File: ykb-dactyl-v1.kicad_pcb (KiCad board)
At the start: 2 copper layers, 55.8 x 58.3 mm, 58 parts, among them IC1 TXU0101DCKR, J1 JST_SH_BM10B-SRSS-TB_1x10-1MP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, J2 JST_SH_BM10B-SRSS-TB_1x10-1MP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, J3 JST_SH_BM10B-SRSS-TB_1x10-1MP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, J4 JST_SH_BM10B-SRSS-TB_1x10-1MP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, J5 JST_SH_BM10B-SRSS-TB_1x10-1MP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, J6 JST_SH_BM10B-SRSS-TB_1x10-1MP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, J7 JST_SH_BM12B-SRSS-TB_1x12-1MP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, J8 MC-121-L124, J9 Conn_ARM_SWD_TagConnect_TC203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

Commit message: Update
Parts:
- removed C1: C, Capacitor_SMD:C_0402_1005Metric
- removed the R1 at (104.9, 94.4)
- added D2: QLS6B-FKW, LED_SMD:LED_Cree-PLCC6_4.7x1.5mm, F.Cu at (114.1, 86.0)
- added J10: Conn_01x05, Connector_PinSocket_2.54mm:PinSocket_1x05_P2.54mm_Vertical, F.Cu at (70.0, 96.0)
- added R4: 10K, Resistor_SMD:R_0402_1005Metric, F.Cu at (64.5, 29.5)
- added R5: 10K, Resistor_SMD:R_0402_1005Metric, F.Cu at (59.2, 33.1)
- added R6: 10K, Resistor_SMD:R_0402_1005Metric, F.Cu at (59.2, 35.1)
- added S6: SKRTLAE010, footprints:SKRTLAE010, F.Cu at (112.2, 79.5)
- J9: value Conn_ARM_SWD_TagConnect_TC2030_NL -> Conn_01x05; footprint Connector:Tag-Connect_TC2030-IDC-NL_2x03_P1.27mm_Vertical -> Connector_PinSocket_2.54mm:PinSocket_1x05_P2.54mm_Vertical; moved to F.Cu
- R1, R2, R3: value 1K -> 600
- moved J9 25.1 mm to (102.3, 97.0)
- moved D1 19.7 mm to (65.6, 85.5), turned to -101.988 degrees
- moved S3 14.0 mm to (93.8, 77.8)
- moved S5 10.4 mm to (67.8, 79.0), turned to -101.988 degrees
- moved S4 7.70 mm to (78.2, 79.3)
- moved S1 6.91 mm to (78.8, 73.3)
- moved J7 4.05 mm to (90.0, 63.0)
- moved J6 3.80 mm to (98.0, 62.5)
- moved J5 3.55 mm to (82.0, 63.0)
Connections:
- net Net-(D1-KB) renamed /MCU/DBG_LED_P
- net Net-(D1-KR-Pad4) renamed /MCU/BAT_STAT_1_P
- net Net-(D1-KR-Pad6) renamed /MCU/BAT_STAT_2_P
- J9 pad 1: +3.3V_SYS -> /MCU/DBG_UART_APPCORE_TX
- J9 pad 2: /MCU/SWDIO -> /MCU/DBG_UART_APPCORE_RX
- J9 pad 3: /MCU/RESET -> /MCU/DBG_UART_NETCORE_TX
- J9 pad 4: /MCU/SWCLK -> /MCU/DBG_UART_NETCORE_RX
- U1 pad P1.2: /MCU/I2C_SDA -> unconnected-(U1B-P1.02-PadP1.2)
- U1 pad P1.4: /MCU/I2C_SCL -> unconnected-(U1B-P1.04-PadP1.4)

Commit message: Update
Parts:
- added D3: RB751S40,115, footprints:RB751S40115, F.Cu at (58.5, 48.6)
- added R23: 47K, Resistor_SMD:R_0402_1005Metric, F.Cu at (57.5, 51.5)
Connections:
- U1 pad P0.13: unconnected-(U1-PadP0.13) -> /MCU/SW_P

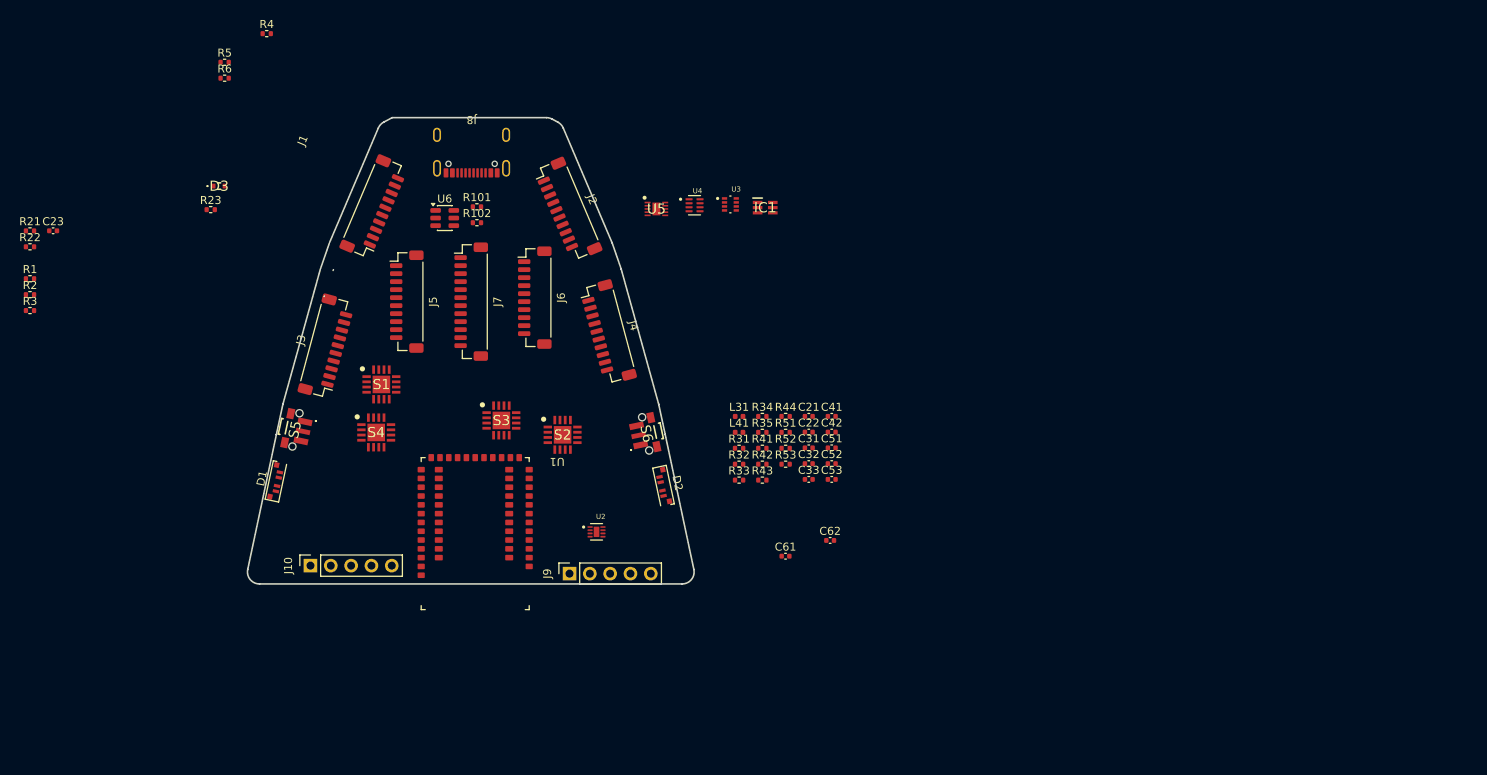
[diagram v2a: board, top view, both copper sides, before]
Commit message: Fix board shape
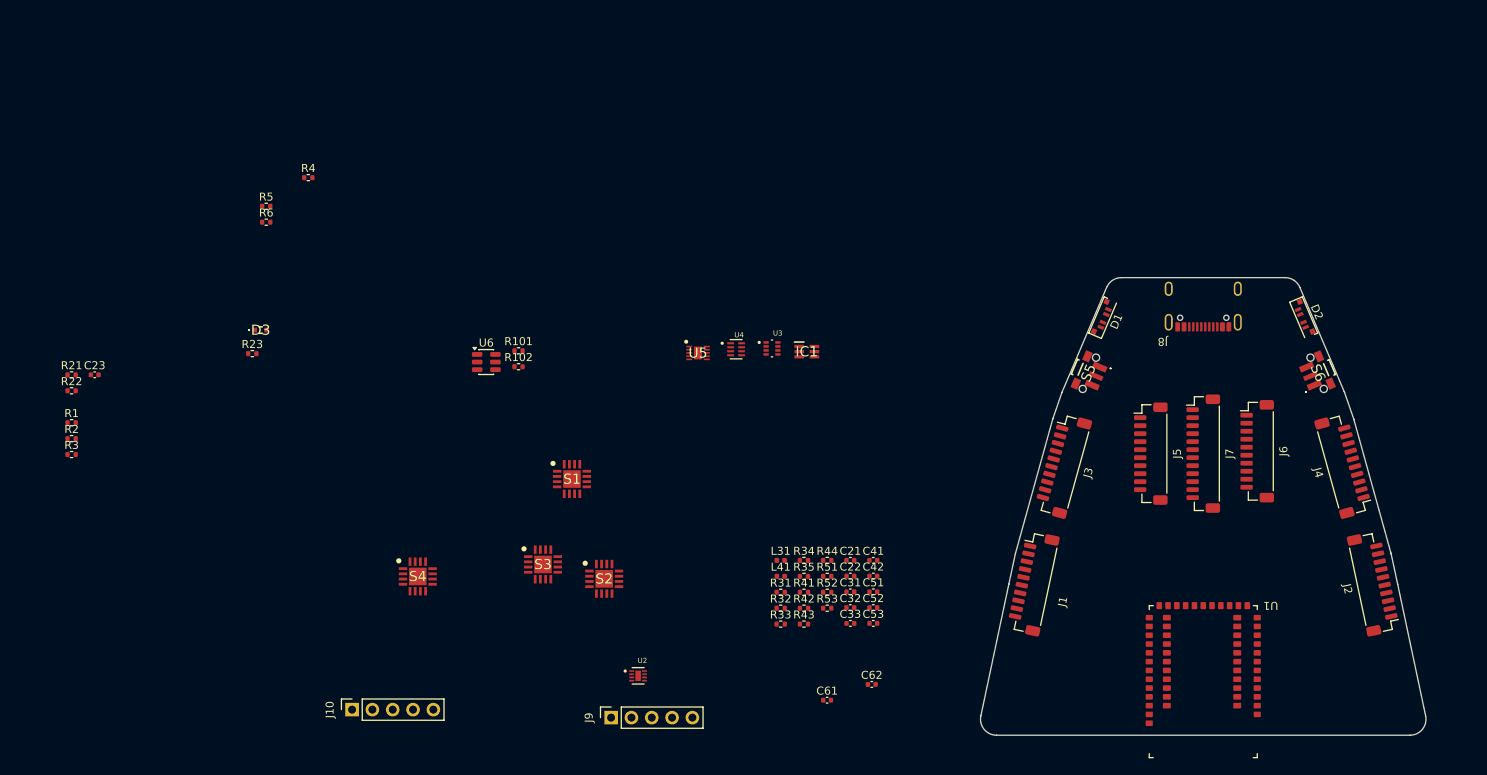
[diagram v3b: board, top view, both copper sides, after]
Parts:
- U1: value holyiot-21069 -> Holyiot-21069
- moved J2 111.0 mm to (202.8, 98.2), turned to 101.989 degrees
- moved D1 105.4 mm to (169.0, 65.0), turned to -113.058 degrees
- moved S5 99.5 mm to (167.0, 71.8), turned to -113.058 degrees
- moved J5 94.9 mm to (175.0, 82.0)
- moved J1 94.8 mm to (160.3, 98.2), turned to -101.988 degrees
- moved J8 94.4 mm to (181.6, 63.0)
- moved J4 93.5 mm to (199.1, 83.5), turned to 105.502 degrees
- moved J7 93.5 mm to (181.6, 82.0)
- moved J3 93.2 mm to (164.0, 83.5), turned to -105.502 degrees
- moved J6 92.3 mm to (188.3, 81.7)
- moved U1 88.8 mm to (181.6, 110.5)
- moved S6 84.3 mm to (196.1, 71.8), turned to 113.058 degrees
- moved D2 82.7 mm to (194.1, 65.0), turned to 113.058 degrees
- moved S1 26.6 mm to (102.7, 85.2)
- moved D3 18.7 mm to (63.7, 66.6)
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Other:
- board size 55.8 x 58.3 mm -> 55.7 x 57.2 mm

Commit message: Fix global nets
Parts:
- U1: value Holyiot-21069 -> holyiot-21069
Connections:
- C23 pad 1: /Power/SHDN -> SHDN
- D3 pad 1: /Power/SW_P -> SW_P
- IC1 pad 4: /MCU/LED_D_0 -> LED_D_0
- J1 pad 5: /MUXes/MUX1_D -> MUX1_D
- J1 pad 7: /MUXes/LED_D_0 -> LED_D_0
- J2 pad 5: /MUXes/MUX1_D -> MUX1_D
- J3 pad 5: /MUXes/MUX2_D -> MUX2_D
- J4 pad 5: /MUXes/MUX2_D -> MUX2_D
- J5 pad 5: /MUXes/MUX3_D -> MUX3_D
- J6 pad 5: /MUXes/MUX3_D -> MUX3_D
- J7 pad 7: /MUXes/MUX4_D -> MUX4_D
- R1 pad 1: /MCU/BAT_STAT_1 -> BAT_STAT_1
- R2 pad 1: /MCU/BAT_STAT_2 -> BAT_STAT_2
- R21 pad 1: /Power/SHDN -> SHDN
- R23 pad 1: /Power/SW_P -> SW_P
- R4 pad 1: /MCU/BAT_STAT_1 -> BAT_STAT_1
- R5 pad 1: /MCU/BAT_STAT_2 -> BAT_STAT_2
- S1 pad 13: /MUXes/MUX1_D -> MUX1_D
- S1 pad 15: /MUXes/MUX1_A2 -> MUX1_A2
- S1 pad 5: /MUXes/MUX1_A0 -> MUX1_A0
- S1 pad 7: /MUXes/MUX1_A1 -> MUX1_A1
- S2 pad 13: /MUXes/MUX2_D -> unconnected-(S2-D-Pad13)
- S2 pad 15: /MUXes/MUX2_A2 -> MUX2_A2
- S2 pad 5: /MUXes/MUX2_A0 -> MUX2_A0
- S2 pad 7: /MUXes/MUX2_A1 -> MUX2_A1
- S3 pad 13: /MUXes/MUX3_D -> MUX3_D
- S3 pad 15: /MUXes/MUX3_A2 -> MUX3_A2
- S3 pad 5: /MUXes/MUX3_A0 -> MUX3_A0
- S3 pad 7: /MUXes/MUX3_A1 -> MUX3_A1
- S4 pad 13: /MUXes/MUX4_D -> MUX4_D
- S4 pad 15: /MUXes/MUX4_A2 -> MUX4_A2
- S4 pad 5: /MUXes/MUX4_A0 -> MUX4_A0
- S4 pad 7: /MUXes/MUX4_A1 -> MUX4_A1
- U1 pad D+: /MCU/USB_DP_P -> USB_DP_P
- U1 pad D-: /MCU/USB_DN_P -> USB_DN_P
- U1 pad P0.10: /MCU/MUX1_A2 -> MUX1_A2
- U1 pad P0.11: /MCU/MUX1_A1 -> MUX1_A1
- U1 pad P0.12: /MCU/MUX1_A0 -> MUX1_A0
- U1 pad P0.13: /MCU/SW_P -> SW_P
- U1 pad P0.14: /MCU/SHDN -> SHDN
- U1 pad P0.17: /MCU/BAT_STAT_1 -> BAT_STAT_1
- U1 pad P0.18: /MCU/BAT_STAT_2 -> BAT_STAT_2
- U1 pad P0.19: /MCU/MUX3_A1 -> MUX3_A1
- U1 pad P0.21: /MCU/MUX3_A0 -> MUX3_A0
- U1 pad P0.22: /MCU/MUX2_A1 -> MUX2_A1
- U1 pad P0.23: /MCU/MUX2_A2 -> MUX2_A2
- U1 pad P0.25: /MCU/MUX4_A0 -> MUX4_A0
- U1 pad P0.29: /MCU/MUX3_A2 -> MUX3_A2
- U1 pad P0.4: /MCU/MUX1_D -> MUX1_D
- U1 pad P0.5: /MCU/MUX2_D -> MUX2_D
- U1 pad P0.6: /MCU/MUX3_D -> MUX3_D
- U1 pad P0.7: /MCU/MUX4_D -> MUX4_D
- U1 pad P0.9: /MCU/MUX2_A0 -> MUX2_A0
- U1 pad P1.7: /MCU/MUX4_A2 -> MUX4_A2
- U1 pad P1.9: /MCU/MUX4_A1 -> MUX4_A1
- U2 pad 7: /Power/SHDN -> SHDN
- U5 pad 3: /Power/BAT_STAT_2 -> BAT_STAT_2
- U5 pad 9: /Power/BAT_STAT_1 -> BAT_STAT_1
- U6 pad 1: /USB/USB_DN_P -> USB_DN_P
- U6 pad 3: /USB/USB_DP_P -> USB_DP_P

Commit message: Place components
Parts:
- added J11: Conn_01x02_MountingPin, Connector_JST:JST_SH_BM02B-SRSS-TB_1x02-1MP_P1.00mm_Vertical, F.Cu at (184.3, 94.8)
- moved C23 155.1 mm to (197.9, 79.0)
- moved R21 155.1 mm to (195.0, 79.0)
- moved R22 155.1 mm to (195.0, 81.0)
- moved D3 137.1 mm to (199.7, 84.5)
- moved R23 137.1 mm to (198.7, 87.0)
- moved R1 134.0 mm to (174.0, 72.0)
- moved R2 134.0 mm to (174.0, 74.0)
- moved R3 134.0 mm to (174.0, 76.0)
- moved J10 124.5 mm to (198.9, 100.5), turned to 11.989 degrees
- moved R5 114.3 mm to (176.5, 73.5)
- moved R6 114.3 mm to (176.5, 75.5)
- moved R4 109.6 mm to (176.5, 72.0)
- moved J9 96.6 mm to (202.9, 99.6), turned to 11.989 degrees
- moved U2 91.8 mm to (198.3, 81.6)
- moved S4 91.8 mm to (175.2, 96.5)
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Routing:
- net GND: vias 0 -> 4

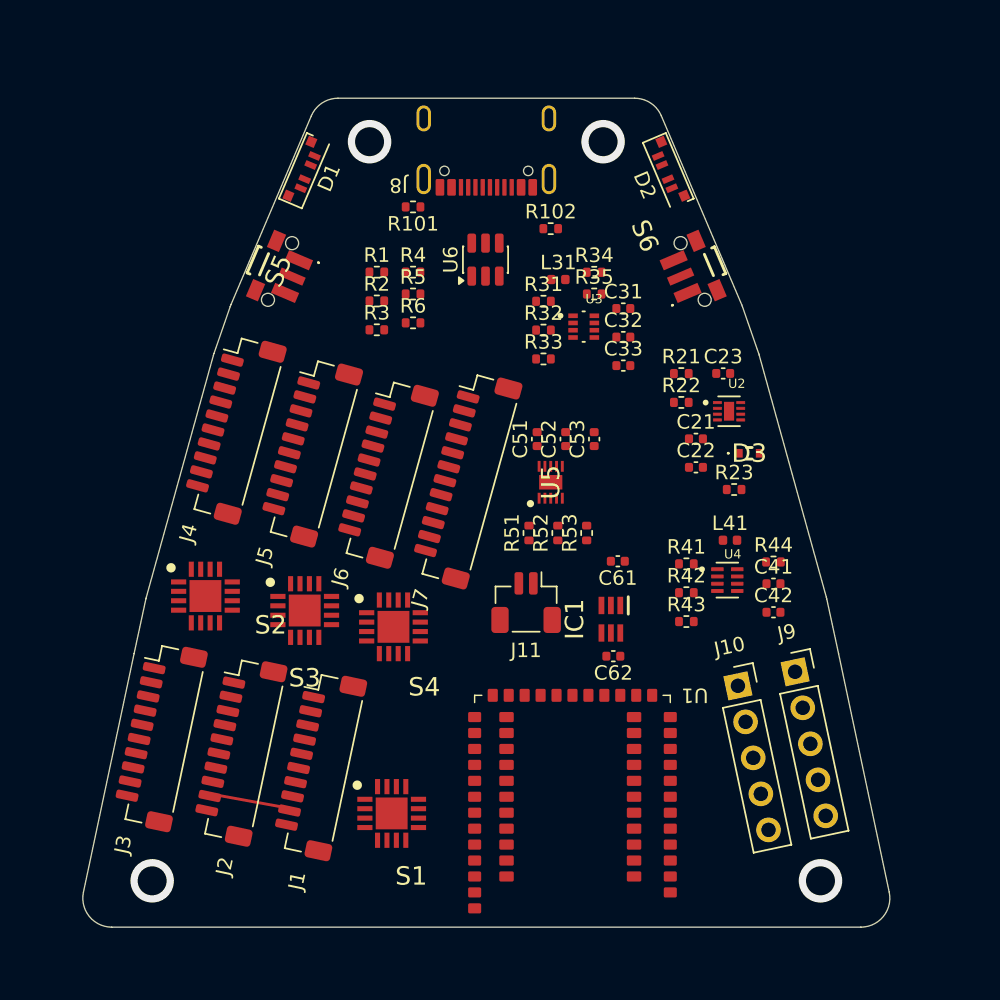
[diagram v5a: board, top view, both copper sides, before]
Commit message: Trace the board
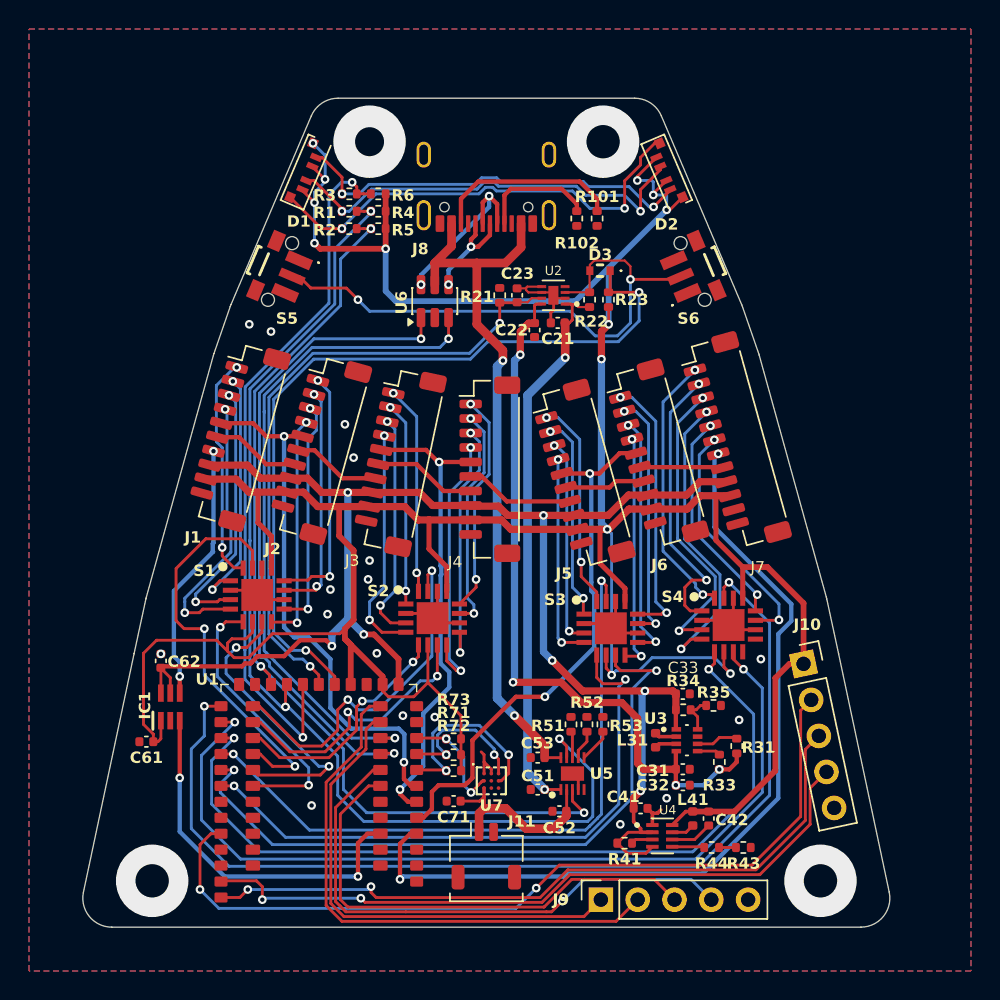
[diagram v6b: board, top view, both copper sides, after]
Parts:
- removed R32, R42: 100K, Resistor_SMD:R_0402_1005Metric
- added C71: 1uF, Capacitor_SMD:C_0402_1005Metric, F.Cu at (179.3, 108.5)
- added R71: 10K, Resistor_SMD:R_0402_1005Metric, F.Cu at (179.3, 105.3)
- added R72: 10K, Resistor_SMD:R_0402_1005Metric, F.Cu at (179.3, 106.4)
- added R73: 10K, Resistor_SMD:R_0402_1005Metric, F.Cu at (179.3, 104.2)
- added U7: LC709203FXE-03MH, footprints:WLCSP9_1P60X1P76_ONS, F.Cu at (181.9, 107.1)
- J11: footprint Connector_JST:JST_SH_BM02B-SRSS-TB_1x02-1MP_P1.00mm_Vertical -> Connector_JST:JST_SHL_SM02B-SHLS-TF_1x02-1MP_P1.00mm_Horizontal
- moved C61 34.8 mm to (158.1, 104.4)
- moved R31 33.5 mm to (198.8, 104.7), turned to -90 degrees
- moved L31 32.5 mm to (193.2, 104.3), turned to 90 degrees
- moved C31 32.1 mm to (195.1, 106.3)
- moved C62 31.2 mm to (159.1, 98.8), turned to 90 degrees
- moved C32 31.2 mm to (195.1, 107.4)
- moved IC1 31.0 mm to (159.8, 102.0), turned to 90 degrees
- moved R34 30.8 mm to (195.1, 102.2), turned to 180 degrees
- moved R33 30.3 mm to (197.6, 105.8), turned to -90 degrees
- moved R35 29.6 mm to (197.2, 101.9)
- moved U3 29.4 mm to (195.4, 104.3)
- moved C52 25.7 mm to (186.6, 109.2), turned to 180 degrees
- moved J3 25.1 mm to (175.5, 85.0)
- moved C51 24.2 mm to (185.1, 107.7), turned to 180 degrees
- moved J1 23.4 mm to (164.4, 83.3), turned to -105.502 degrees
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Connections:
- S1 pad 13: MUX1_D -> +3.3V_SYS
- S2 pad 13: unconnected-(S2-D-Pad13) -> +3.3V_SYS
- S3 pad 13: MUX3_D -> +3.3V_SYS
- S4 pad 13: MUX4_D -> +3.3V_SYS
- U1 pad P1.0: unconnected-(U1B-P1.00-PadP1.0) -> SCL
- U1 pad P1.1: unconnected-(U1B-P1.01-PadP1.1) -> SDA
- U1 pad P1.2: unconnected-(U1B-P1.02-PadP1.2) -> ALARMB
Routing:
- net +3.3V_SYS: track 0.03 -> 243.7 mm, vias 0 -> 13
- net +5V_SYS: track 0.00 -> 110.4 mm, vias 0 -> 7
- net BAT_STAT_1: track 0.00 -> 75.5 mm, vias 0 -> 3
- net MUX4_A2: track 0.00 -> 70.1 mm, vias 0 -> 2
- net BAT_STAT_2: track 0.00 -> 66.3 mm, vias 0 -> 3
- net MUX4_A1: track 0.00 -> 60.9 mm, vias 0 -> 2
- net MUX4_D: track 0.00 -> 58.7 mm, vias 0 -> 2
- net /MCU/RESET: track 0.00 -> 57.8 mm, vias 0 -> 2
- net MUX4_A0: track 0.00 -> 57.6 mm, vias 0 -> 2
- net SW_P: track 0.00 -> 55.2 mm, vias 0 -> 2
- net VCC_SYS: track 0.00 -> 50.7 mm, vias 0 -> 4
- net +5V_USB: track 0.00 -> 50.3 mm, vias 0 -> 2
- net /MCU/SWCLK: track 0.00 -> 49.6 mm, vias 0 -> 2
- net /MCU/DBG_LED: track 0.00 -> 49.2 mm, vias 0 -> 2
- net /MCU/SWDIO: track 0.00 -> 48.2 mm, vias 0 -> 2
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- added copper zone on B.Cu, net GND
- added copper zone on F.Cu, net GND
